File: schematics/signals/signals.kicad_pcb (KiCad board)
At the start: 4 copper layers, 31.8 x 25.4 mm, 30 parts, among them J1 Conditioned, J2 Sensors, U1 INA849D, U2 OPA2182, U3 INA849D

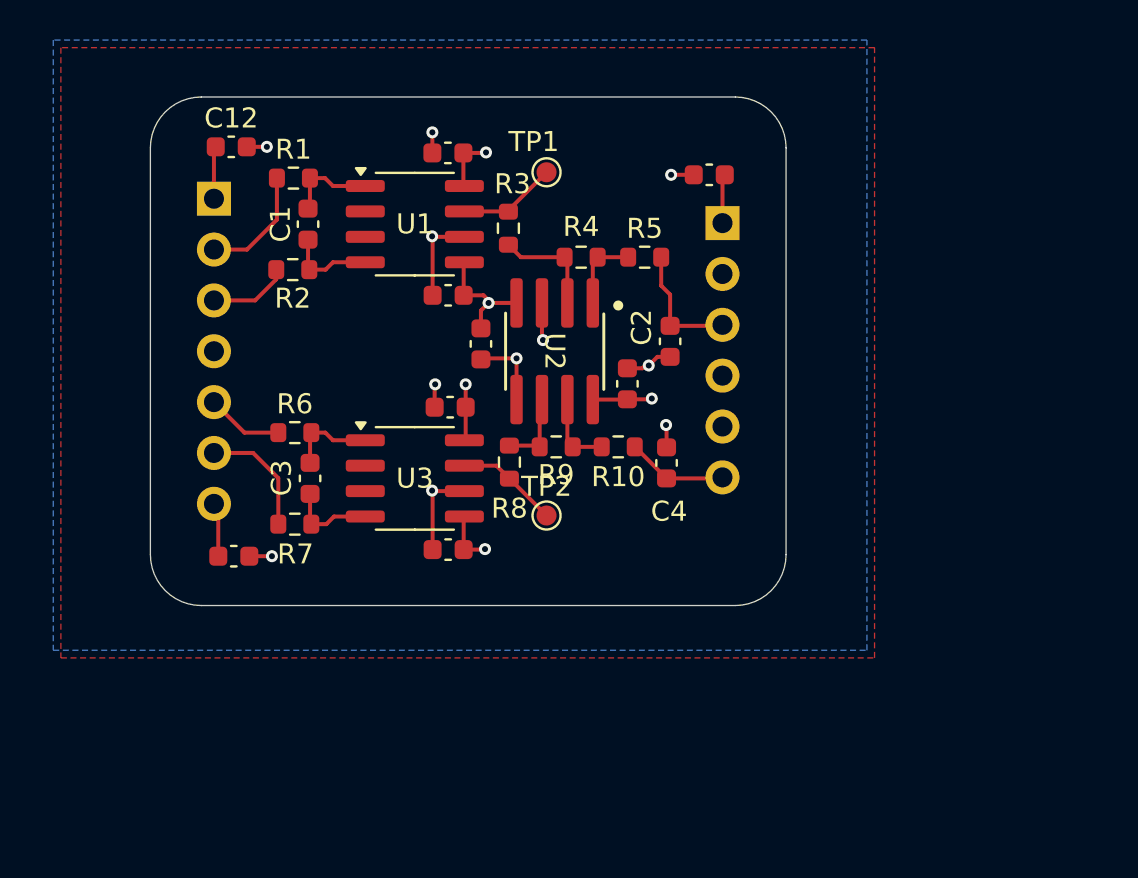
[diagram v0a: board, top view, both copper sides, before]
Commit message: update(signals): review
1. Add notes to schematics
2. Switch out INA849 for AD8422ARMZ to help with input bias current
3. Add open R_g pads to AD8422
4. Add dip switches for R_f in OPA circuit
5. Fix pinout
	Initial abalmos and I discussed switching the pinout so the
	input to the ADC was the correct direction and the inversion was
	at the inputs to the INA. This cannot work due to the
	asymmetrical supplies

TODO:
1. Update motherboard
2. Add MFB bessel filter
3. Make slightly bigger in case of later revisions (optional)
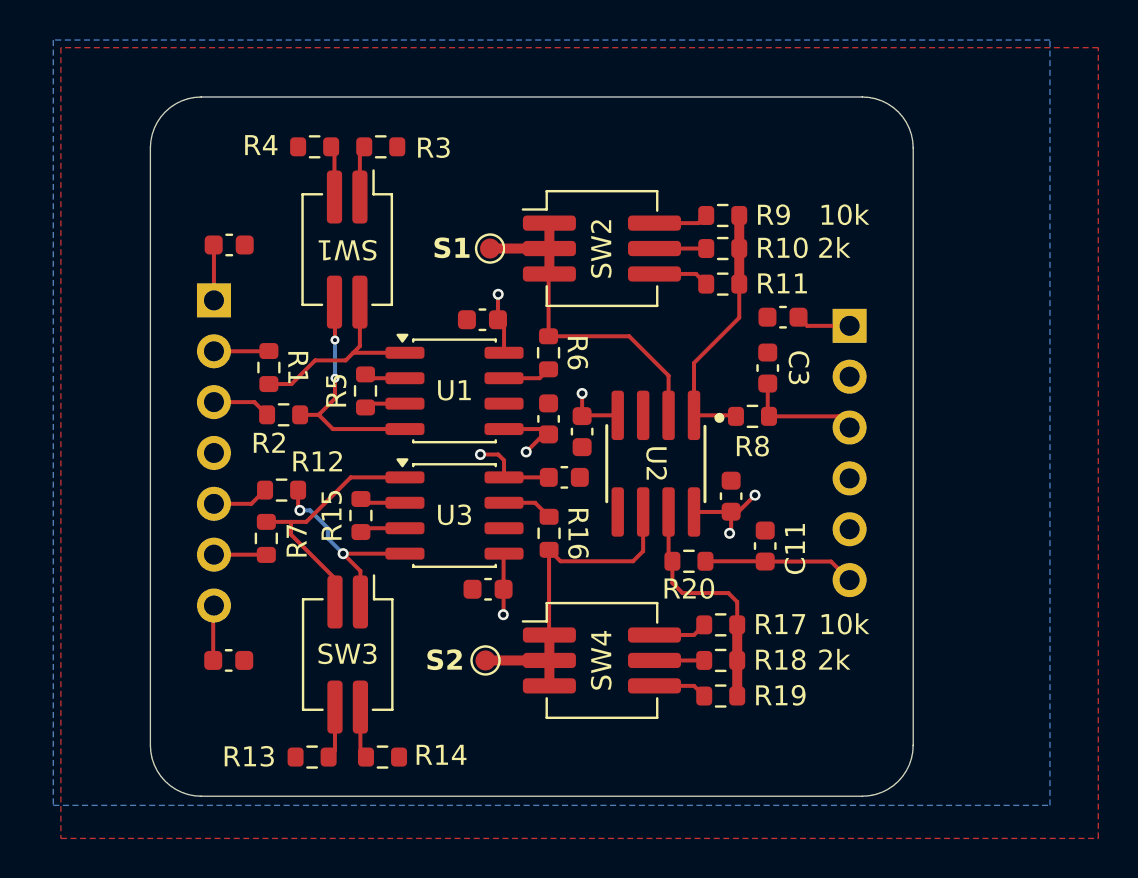
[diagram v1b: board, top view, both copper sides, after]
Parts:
- removed the C1 at (185.1, 49.5)
- removed the C2 at (203.1, 55.3)
- removed the C4 at (203.0, 61.4)
- removed the C6 at (192.0, 45.9)
- removed the R6 at (184.4, 59.9)
- added C11: 0.62nF, Capacitor_SMD:C_0603_1608Metric, F.Cu at (207.9, 65.5)
- added C9: 0.1uF, Capacitor_SMD:C_0603_1608Metric, F.Cu at (194.1, 67.7)
- added R11: 2k, Resistor_SMD:R_0603_1608Metric, F.Cu at (205.8, 52.5)
- added R12: 100, Resistor_SMD:R_0603_1608Metric, F.Cu at (183.7, 62.7)
- added R13: 10M, Resistor_SMD:R_0603_1608Metric, F.Cu at (185.3, 76.1)
- added R14: 10M, Resistor_SMD:R_0603_1608Metric, F.Cu at (188.8, 76.1)
- added R15: Rg, Resistor_SMD:R_0603_1608Metric, F.Cu at (187.7, 64.0)
- added R16: 10k, Resistor_SMD:R_0603_1608Metric, F.Cu at (197.1, 64.9)
- added R17: 10k, Resistor_SMD:R_0603_1608Metric, F.Cu at (205.7, 69.5)
- added R18: 2k, Resistor_SMD:R_0603_1608Metric, F.Cu at (205.7, 71.2)
- added R19: 2k, Resistor_SMD:R_0603_1608Metric, F.Cu at (205.7, 73.0)
- added R20: 1k, Resistor_SMD:R_0603_1608Metric, F.Cu at (204.1, 66.3)
- added R3: 10M, Resistor_SMD:R_0603_1608Metric, F.Cu at (188.7, 45.6)
- added SW1: Returns, Button_Switch_SMD:SW_DIP_SPSTx02_Slide_KingTek_DSHP02TJ_W5.25mm_P1.27mm_JPin, F.Cu at (187.0, 50.7)
- added SW2: Feedbacks, Button_Switch_SMD:SW_DIP_SPSTx03_Slide_KingTek_DSHP03TJ_W5.25mm_P1.27mm_JPin, F.Cu at (199.7, 50.7)
- added SW3: Returns, Button_Switch_SMD:SW_DIP_SPSTx02_Slide_KingTek_DSHP02TJ_W5.25mm_P1.27mm_JPin, F.Cu at (187.0, 71.0)
- added SW4: Feedbacks, Button_Switch_SMD:SW_DIP_SPSTx03_Slide_KingTek_DSHP03TJ_W5.25mm_P1.27mm_JPin, F.Cu at (199.7, 71.2)
- C1: renamed from C9; value 10uF -> 0.1uF
- C10: value 10uF -> 0.1uF
- C2: renamed from C5; value 10uF -> 0.1uF
- C3: value 10nF -> 0.62nF
- C4: renamed from C7; value 10uF -> 0.1uF
- C5: renamed from C8; value 10uF -> 0.1uF
- R1, R2, R7: value 1k -> 100
- R10: value 1k -> 2k
- R4: value 2k -> 10M
- R5: value 1k -> Rg
- R8: value 10k -> 1k
- R9: value 2k -> 10k
- U1, U3: value INA849D -> AD8422ARMZ
- moved C3 23.5 mm to (208.0, 56.6), turned to 90 degrees
- moved R5 15.5 mm to (187.9, 57.8), turned to 90 degrees
- moved R4 14.4 mm to (185.4, 45.6), turned to 180 degrees
- moved R9 14.2 mm to (205.8, 49.0)
- moved R8 12.4 mm to (207.3, 59.1), turned to 0 degrees
- moved R10 11.2 mm to (205.8, 50.7)
- moved R1 9.54 mm to (183.1, 56.6), turned to -90 degrees
- moved U1 8.56 mm to (192.4, 57.8)
- moved J2 8.16 mm to (212.1, 54.5)
- moved C8 8.01 mm to (208.8, 54.1)
- moved C1 7.95 mm to (197.1, 59.2), turned to 90 degrees
- moved TP2 7.85 mm to (193.9, 71.2)
- moved C4 7.64 mm to (206.2, 63.0)
- moved U2 7.55 mm to (202.4, 61.4)
- moved R2 7.27 mm to (183.8, 59.0)
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- renumbered C12 to C6, C11 to C7, C13 to C8, J2 to J1, J1 to J2, R3 to R6
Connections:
- C10 pad 1: -3V3 -> +12V
- C3 pad 1: Net-(U3--) -> /Sc1-
- C3 pad 2: Net-(U3-+) -> GND
- J1 pad 5: /S2- -> /S2+
- J1 pad 6: /S2+ -> /S2-
- R10 pad 2: /Sc2- -> Net-(R10-Pad2)
- R4 pad 1: Net-(U2A--) -> Net-(R4-Pad1)
- R4 pad 2: Net-(R4-Pad2) -> GND
- R5 pad 1: Net-(R4-Pad2) -> unconnected-(R5-Pad1)
- R5 pad 2: /Sc1- -> unconnected-(R5-Pad2)
- R6 pad 1: Net-(R3-Pad1) -> Net-(R6-Pad1)
- R7 pad 1: /S2+ -> /S2-
- R7 pad 2: Net-(U3-+) -> Net-(U3--)
- R8 pad 1: Net-(R8-Pad1) -> Net-(R10-Pad2)
- R8 pad 2: Net-(U2B--) -> /Sc1-
- R9 pad 1: Net-(U2B--) -> Net-(R9-Pad1)
- R9 pad 2: Net-(R10-Pad1) -> Net-(R10-Pad2)
- TP1 pad 1: Net-(R3-Pad1) -> Net-(U2A--)
- TP2 pad 1: Net-(R8-Pad1) -> Net-(U2B--)
- U1 pad 2: unconnected-(U1-Rg-Pad2) -> unconnected-(R5-Pad2)
- U1 pad 3: unconnected-(U1-Rg-Pad3) -> unconnected-(R5-Pad1)
- U1 pad 7: Net-(R3-Pad1) -> Net-(R6-Pad1)
- U2 pad 1: Net-(R4-Pad2) -> Net-(R10-Pad2)
- U2 pad 7: Net-(R10-Pad1) -> Net-(R17-Pad2)
- U3 pad 7: Net-(R8-Pad1) -> Net-(R16-Pad1)
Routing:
- net GND: track 23.6 -> 0.00 mm, vias 11 -> 0
- net Net-(U2B--): track 3.95 -> 17.1 mm
- net Net-(R10-Pad2): track 0.00 -> 13.0 mm
- net Net-(R17-Pad2): track 0.00 -> 12.1 mm
- net Net-(U2A--): track 5.41 -> 17.4 mm
- net Net-(U3--): track 4.39 -> 12.8 mm
- net Net-(U1-+): track 4.47 -> 11.5 mm, vias 0 -> 2
- net Net-(U3-+): track 4.39 -> 10.3 mm, vias 0 -> 2
- net Net-(U1--): track 4.49 -> 10.1 mm
- net Net-(R8-Pad1): track 5.13 -> 0.00 mm
- net Net-(R4-Pad2): track 3.91 -> 0.00 mm
- net /S2+: track 6.03 -> 2.84 mm
- net /S1-: track 5.84 -> 2.77 mm
- net Net-(R11-Pad1): track 0.00 -> 2.79 mm
- net Net-(R9-Pad1): track 0.00 -> 2.74 mm
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- added copper zone on F.Cu, net GND
- removed copper zone on F.Cu, net (none)
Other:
- board size 31.8 x 25.4 mm -> 38.1 x 34.9 mm

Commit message: update(motherboard): fix from signals review
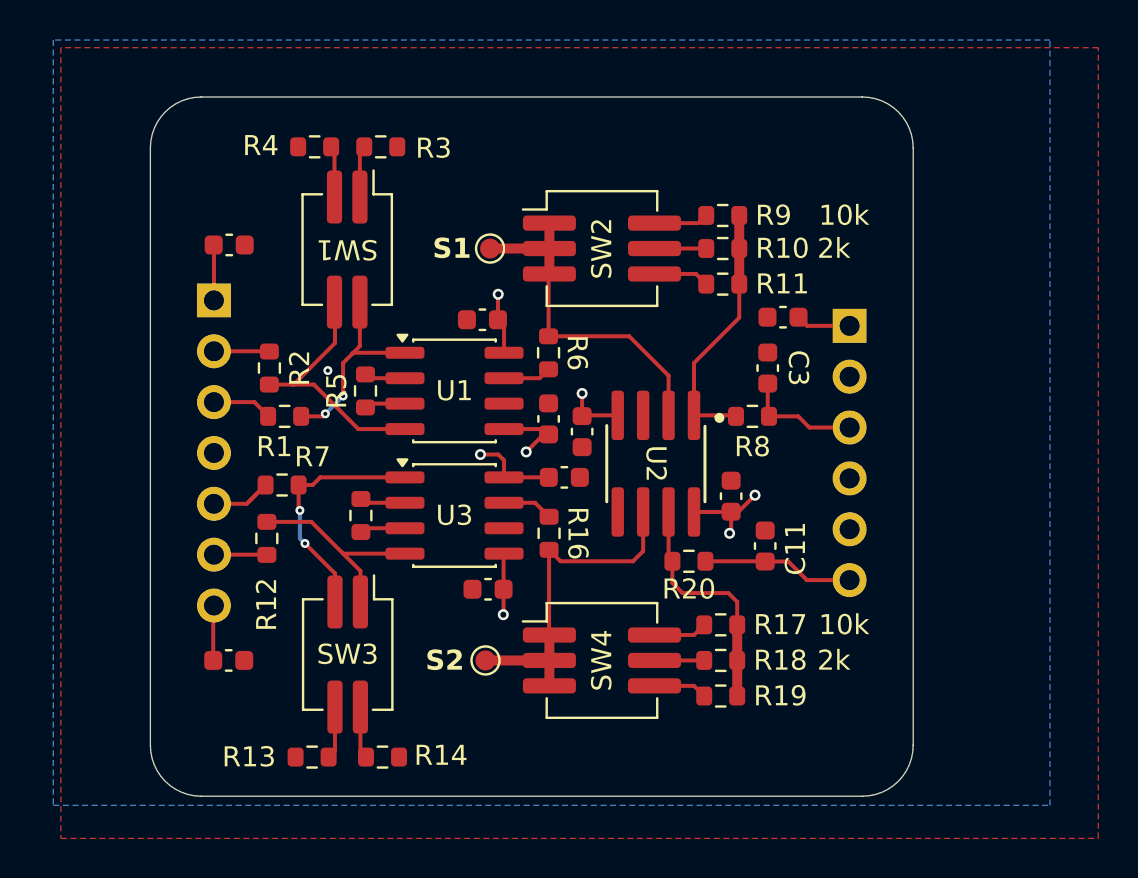
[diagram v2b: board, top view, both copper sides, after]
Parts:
- moved R7 2.78 mm to (183.8, 62.5), turned to 0 degrees
- moved R1 2.56 mm to (183.9, 59.1), turned to 0 degrees
- moved R12 2.52 mm to (183.0, 65.2), turned to 90 degrees
- moved R2 2.44 mm to (183.1, 56.6), turned to -90 degrees
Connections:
- J1 pad 2: /S1- -> /S1+
- J1 pad 3: /S1+ -> /S1-
- J1 pad 5: /S2+ -> /S2-
- J1 pad 6: /S2- -> /S2+
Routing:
- net /S2-: track 2.62 -> 4.14 mm
- net Net-(U1-+): track 11.5 -> 12.7 mm, vias 2 -> 0
- net Net-(U3--): track 12.8 -> 12.1 mm, vias 0 -> 2
- net GND: track 0.00 -> 0.49 mm, vias 0 -> 1
- net Net-(U1--): track 10.1 -> 10.2 mm, vias 0 -> 2
- net Net-(U3-+): vias 2 -> 0

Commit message: production: exported for jlc, had to change some parts for stocking
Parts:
- C6, C7, C8: footprint Capacitor_SMD:C_0603_1608Metric -> Capacitor_SMD:C_0805_2012Metric
- U1, U3: footprint Package_SO:SOIC-8_3.9x4.9mm_P1.27mm -> Package_SO:MSOP-8_3x3mm_P0.65mm
- moved C3 1.12 mm to (207.3, 57.5), turned to 180 degrees
- moved C8 0.28 mm to (208.7, 54.4)
- moved C6 0.23 mm to (181.4, 50.5)
- moved C7 0.18 mm to (181.3, 71.2)
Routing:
- net GND: track 0.49 -> 3.25 mm, vias 1 -> 9
- net +12V: track 10.2 -> 12.6 mm
- net -3V3: track 12.6 -> 14.8 mm
- net Net-(U1--): track 10.2 -> 11.4 mm
- net Net-(U1-+): track 12.7 -> 13.8 mm
- net Net-(U3--): track 12.1 -> 13.1 mm
- net Net-(U3-+): track 10.3 -> 11.3 mm
- net unconnected-(R5-Pad2): track 2.05 -> 2.81 mm
- net unconnected-(R15-Pad2): track 2.28 -> 3.04 mm
- net unconnected-(R15-Pad1): track 2.28 -> 3.04 mm
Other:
- board text added: "Signals rev1.1 07/06/2026"
- board text removed: "Signals v1.0"

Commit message: release: 'LCSC Part #' and 'FT Rotation Offset'
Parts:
- R11, R19: value 2k -> Rf

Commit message: feat(signals): bessel filter
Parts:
- added C12: 220pF, Capacitor_SMD:C_0603_1608Metric, F.Cu at (204.6, 68.8)
- added C13: 100pF, Capacitor_SMD:C_0603_1608Metric, F.Cu at (201.8, 66.3)
- C11: value 0.62nF -> 0.1uF
- C3: value 0.62nF -> 100pF
- C9: value 0.1uF -> 220pF
- R10: value 2k -> 6.65k
- R11: value Rf -> 100
- R16, R6: value 10k -> 33.2k
- R17, R9: value 10k -> 6.65k
- R18: value 2k -> ~
- R19: value Rf -> 6.65k
- R20: value 1k -> 6.65k
- R7: value 100 -> 6.65k
- R8: value 1k -> ~
- moved R11 24.8 mm to (183.1, 62.5)
- moved R7 22.3 mm to (201.6, 49.1)
- moved C11 15.4 mm to (193.1, 61.5), turned to 180 degrees
- moved C9 15.0 mm to (200.6, 54.2), turned to 90 degrees
- moved R8 10.1 mm to (201.6, 50.7)
- moved R6 9.56 mm to (201.6, 47.4), turned to 0 degrees
- moved R16 8.79 mm to (202.0, 72.2), turned to 0 degrees
- moved C10 6.65 mm to (193.0, 66.7), turned to 180 degrees
- moved R19 6.29 mm to (201.0, 68.8), turned to 90 degrees
- moved R17 5.67 mm to (202.0, 73.8)
- moved R18 5.58 mm to (202.0, 75.4)
- moved TP2 5.46 mm to (199.1, 69.6)
- moved R9 5.40 mm to (204.2, 54.2), turned to -90 degrees
- moved TP1 5.31 mm to (198.8, 53.3)
- moved R10 4.86 mm to (202.4, 54.2), turned to -90 degrees
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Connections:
- C10 pad 1: +12V -> -3V3
- C11 pad 1: /Sc2- -> +12V
- C3 pad 1: /Sc1- -> Net-(U2A--)
- C3 pad 2: GND -> /Sc1-
- C9 pad 1: -3V3 -> GND
- C9 pad 2: GND -> Net-(C9-Pad2)
- R10 pad 1: Net-(R10-Pad1) -> Net-(C9-Pad2)
- R10 pad 2: Net-(R10-Pad2) -> Net-(U2A--)
- R11 pad 1: Net-(R11-Pad1) -> /S2-
- R11 pad 2: Net-(R10-Pad2) -> Net-(U3--)
- R16 pad 2: Net-(U2B--) -> Net-(C12-Pad2)
- R17 pad 2: Net-(R17-Pad2) -> Net-(C12-Pad2)
- R18 pad 2: Net-(R17-Pad2) -> Net-(C12-Pad2)
- R19 pad 1: Net-(R19-Pad1) -> Net-(C12-Pad2)
- R19 pad 2: Net-(R17-Pad2) -> Net-(U2B--)
- R20 pad 1: Net-(R17-Pad2) -> Net-(C12-Pad2)
- R6 pad 2: Net-(U2A--) -> Net-(C9-Pad2)
- R7 pad 1: /S2- -> Net-(R7-Pad1)
- R7 pad 2: Net-(U3--) -> Net-(C9-Pad2)
- R8 pad 1: Net-(R10-Pad2) -> Net-(R8-Pad1)
- R8 pad 2: /Sc1- -> Net-(C9-Pad2)
- R9 pad 1: Net-(R9-Pad1) -> Net-(C9-Pad2)
- R9 pad 2: Net-(R10-Pad2) -> /Sc1-
- SW2 pad 1: Net-(U2A--) -> Net-(SW2-Pad1)
- SW2 pad 2: Net-(U2A--) -> Net-(SW2-Pad1)
- SW2 pad 3: Net-(U2A--) -> Net-(SW2-Pad1)
- SW2 pad 4: Net-(R11-Pad1) -> Net-(R8-Pad1)
- SW2 pad 5: Net-(R10-Pad1) -> Net-(R7-Pad1)
- SW2 pad 6: Net-(R9-Pad1) -> Net-(R6-Pad1)
- SW3 pad 1: Net-(U3-+) -> Net-(R13-Pad1)
- SW3 pad 2: Net-(U3--) -> Net-(R14-Pad1)
- SW3 pad 3: Net-(R13-Pad1) -> Net-(U3-+)
- SW3 pad 4: Net-(R14-Pad1) -> Net-(U3--)
- SW4 pad 1: Net-(U2B--) -> Net-(SW4-Pad1)
- SW4 pad 2: Net-(U2B--) -> Net-(SW4-Pad1)
- SW4 pad 3: Net-(U2B--) -> Net-(SW4-Pad1)
- SW4 pad 4: Net-(R19-Pad1) -> Net-(R18-Pad1)
- SW4 pad 5: Net-(R18-Pad1) -> Net-(R17-Pad1)
- SW4 pad 6: Net-(R17-Pad1) -> Net-(R16-Pad1)
- TP1 pad 1: Net-(U2A--) -> Net-(C9-Pad2)
- TP2 pad 1: Net-(U2B--) -> Net-(C12-Pad2)
- U1 pad 7: Net-(R6-Pad1) -> Net-(SW2-Pad1)
- U2 pad 1: Net-(R10-Pad2) -> /Sc1-
- U2 pad 7: Net-(R17-Pad2) -> /Sc2-
- U3 pad 7: Net-(R16-Pad1) -> Net-(SW4-Pad1)
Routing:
- net GND: track 3.25 -> 18.9 mm, vias 9 -> 19
- net Net-(SW4-Pad1): track 0.00 -> 14.3 mm
- net Net-(U2A--): track 17.4 -> 4.08 mm
- net Net-(SW2-Pad1): track 0.00 -> 13.3 mm
- net Net-(R10-Pad2): track 13.0 -> 0.00 mm
- net Net-(U2B--): track 17.1 -> 4.11 mm
- net Net-(R17-Pad2): track 12.1 -> 0.00 mm
- net Net-(C9-Pad2): track 0.00 -> 11.9 mm
- net Net-(C12-Pad2): track 0.00 -> 11.6 mm
- net /Sc1-: track 5.92 -> 12.3 mm
- net /Sc2-: track 7.59 -> 13.5 mm
- net +12V: track 12.6 -> 8.04 mm
- net -3V3: track 14.8 -> 10.8 mm
- net Net-(R11-Pad1): track 2.79 -> 0.00 mm
- net Net-(R8-Pad1): track 0.00 -> 2.79 mm
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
